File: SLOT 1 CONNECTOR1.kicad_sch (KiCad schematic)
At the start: 10 parts, among them J33 Slot1, U24 MAX1617 ME

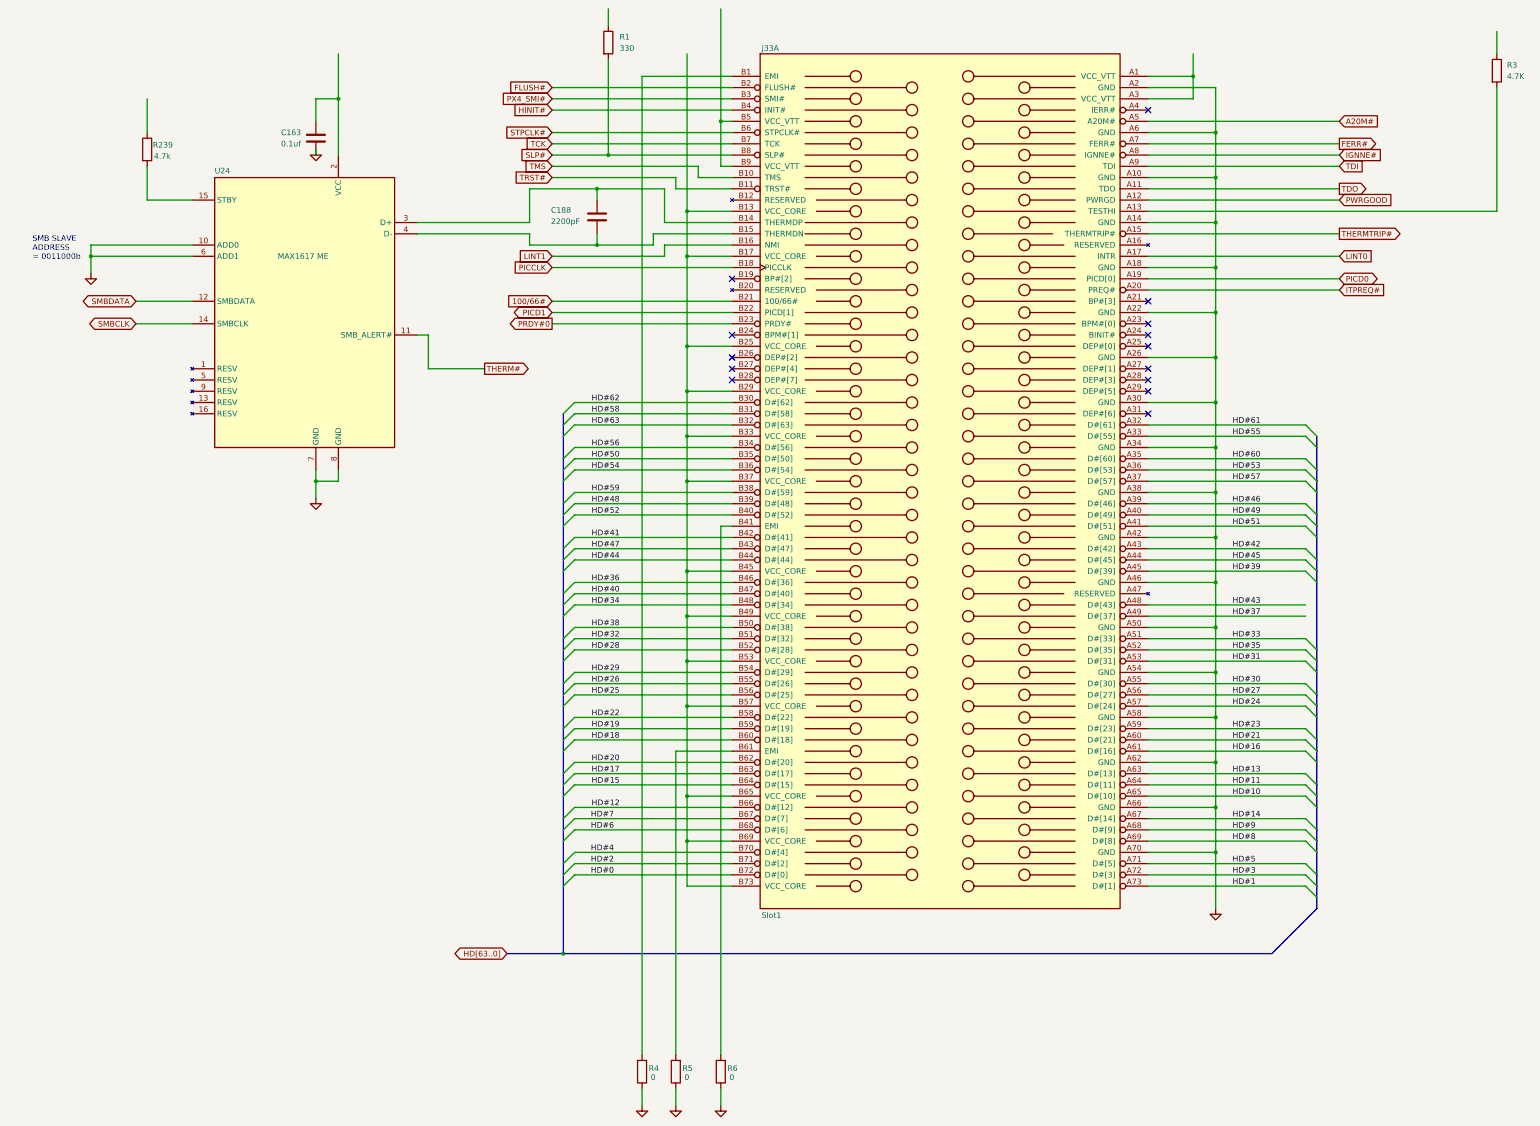
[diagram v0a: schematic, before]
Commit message: Page 3, 4 completed
perfect 1:1 symbols added: Slot1, MAX1617, Jumper
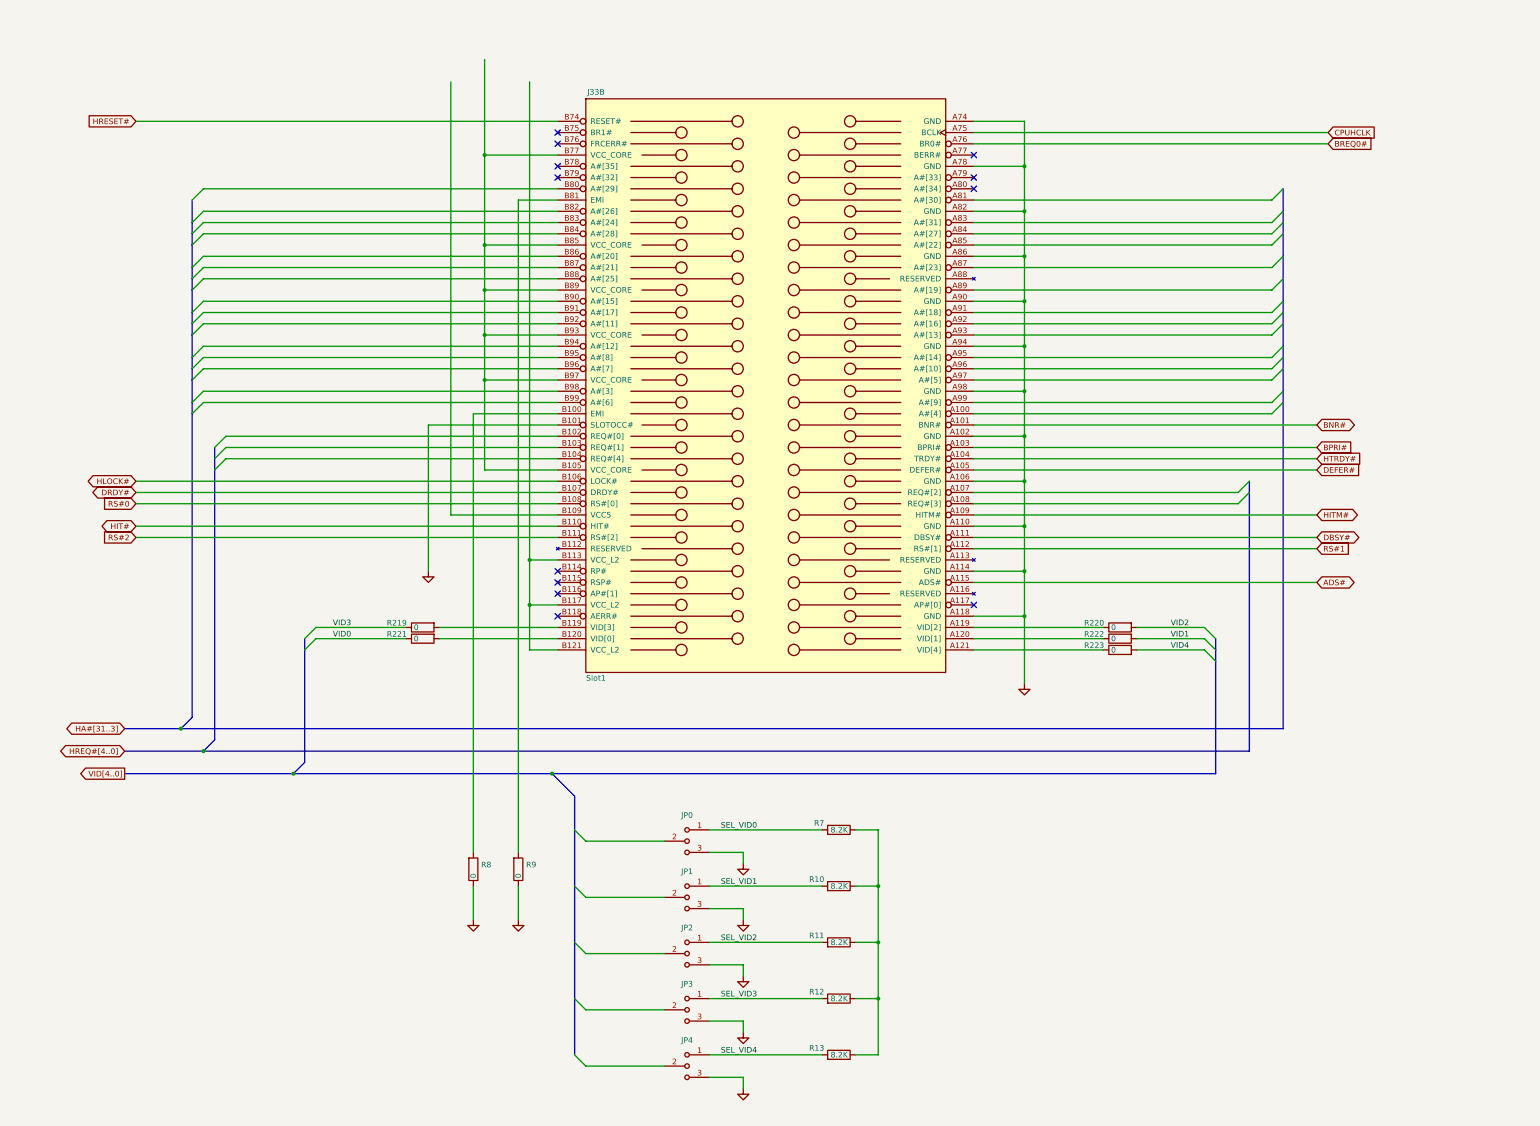
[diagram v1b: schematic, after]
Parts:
- removed C163: 0.1uf, Capacitor_SMD:C_0201_0603Metric, symbol Device:C
- removed C188: 2200pF, Capacitor_SMD:C_0201_0603Metric, symbol Device:C
- removed J33: Slot1, symbol P2-3_era:Slot1
- removed R1: 330, Resistor_SMD:R_0201_0603Metric, symbol Device:R
- removed R239: 4.7k, Resistor_SMD:R_0201_0603Metric, symbol Device:R
- removed R3: 4.7K, Resistor_SMD:R_0201_0603Metric, symbol Device:R
- removed R4, R5, R6: 0, Resistor_SMD:R_0201_0603Metric, symbol Device:R
- removed U24: MAX1617 ME, Package_SO:QSOP-16_3.9x4.9mm_P0.635mm, symbol P2-3_era:MAX1617_ME
- added J33: Slot1, symbol P2-3_era:Slot1
- added JP0, JP1, JP2, JP3, JP4: Jumper_3_Open, symbol P2-3_era:Jumper_3_Open
- added R10, R11, R12, R13, R7: 8.2K, symbol Device:R
- added R219, R220, R221, R222, R223, R8, R9: 0, Resistor_SMD:R_0201_0603Metric, symbol Device:R
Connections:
- net GND: now also J33.A102 (GND), J33.A106 (GND), J33.A110 (GND), J33.A114 (GND), J33.A118 (GND), J33.A74 (GND), J33.A78 (GND), J33.A82 (GND), J33.A86 (GND), J33.A90 (GND), J33.A94 (GND), J33.A98 (GND), J33.B101 (SLOTOCC#), JP0.3 (B), JP1.3 (B), JP2.3 (B), JP3.3 (B), JP4.3 (B), R8.1, R9.1
- new net: R10.1, R11.1, R12.1, R13.1, R7.1
- new net: J33.B119 (VID[3]), R219.2
- new net: J33.A121 (VID[4]), R223.1
- new net: J33.A119 (VID[2]), R220.1
- new net: J33.A120 (VID[1]), R222.1
- new net: J33.B100 (EMI), R8.2
- new net: J33.B105 (VCC_CORE), J33.B77 (VCC_CORE), J33.B85 (VCC_CORE), J33.B89 (VCC_CORE), J33.B93 (VCC_CORE), J33.B97 (VCC_CORE)
- new net: J33.B113 (VCC_L2), J33.B117 (VCC_L2), J33.B121 (VCC_L2)
- new net: J33.B120 (VID[0]), R221.2
- new net: J33.B81 (EMI), R9.2
- new net ADS#: J33.A115 (ADS#)
- new net BNR#: J33.A101 (BNR#)
- new net BPRI#: J33.A103 (BPRI#)
- new net BREQ0#: J33.A76 (BR0#)
- new net CPUHCLK: J33.A75 (BCLK)
- new net DBSY#: J33.A111 (DBSY#)
- new net DEFER#: J33.A105 (DEFER#)
- new net DRDY#: J33.B107 (DRDY#)
- new net HIT#: J33.B110 (HIT#)
- new net HITM#: J33.A109 (HITM#)
- new net HLOCK#: J33.B106 (LOCK#)
- new net HRESET#: J33.B74 (RESET#)
- new net HTRDY#: J33.A104 (TRDY#)
- new net RS#0: J33.B108 (RS#[0])
- new net RS#1: J33.A112 (RS#[1])
- new net RS#2: J33.B111 (RS#[2])
- new net SEL_VID0: JP0.1 (A), R7.2
- new net SEL_VID1: JP1.1 (A), R10.2
- new net SEL_VID2: JP2.1 (A), R11.2
- new net SEL_VID3: JP3.1 (A), R12.2
- new net SEL_VID4: JP4.1 (A), R13.2
- new net VID0: R221.1
- new net VID1: R222.2
- new net VID2: R220.2
- new net VID3: R219.1
- new net VID4: R223.2
- no-connect marks 14 -> 12
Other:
- note removed: "SMB SLAVE ADDRESS = 0011000b"

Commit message: page 3 4 clickable links added
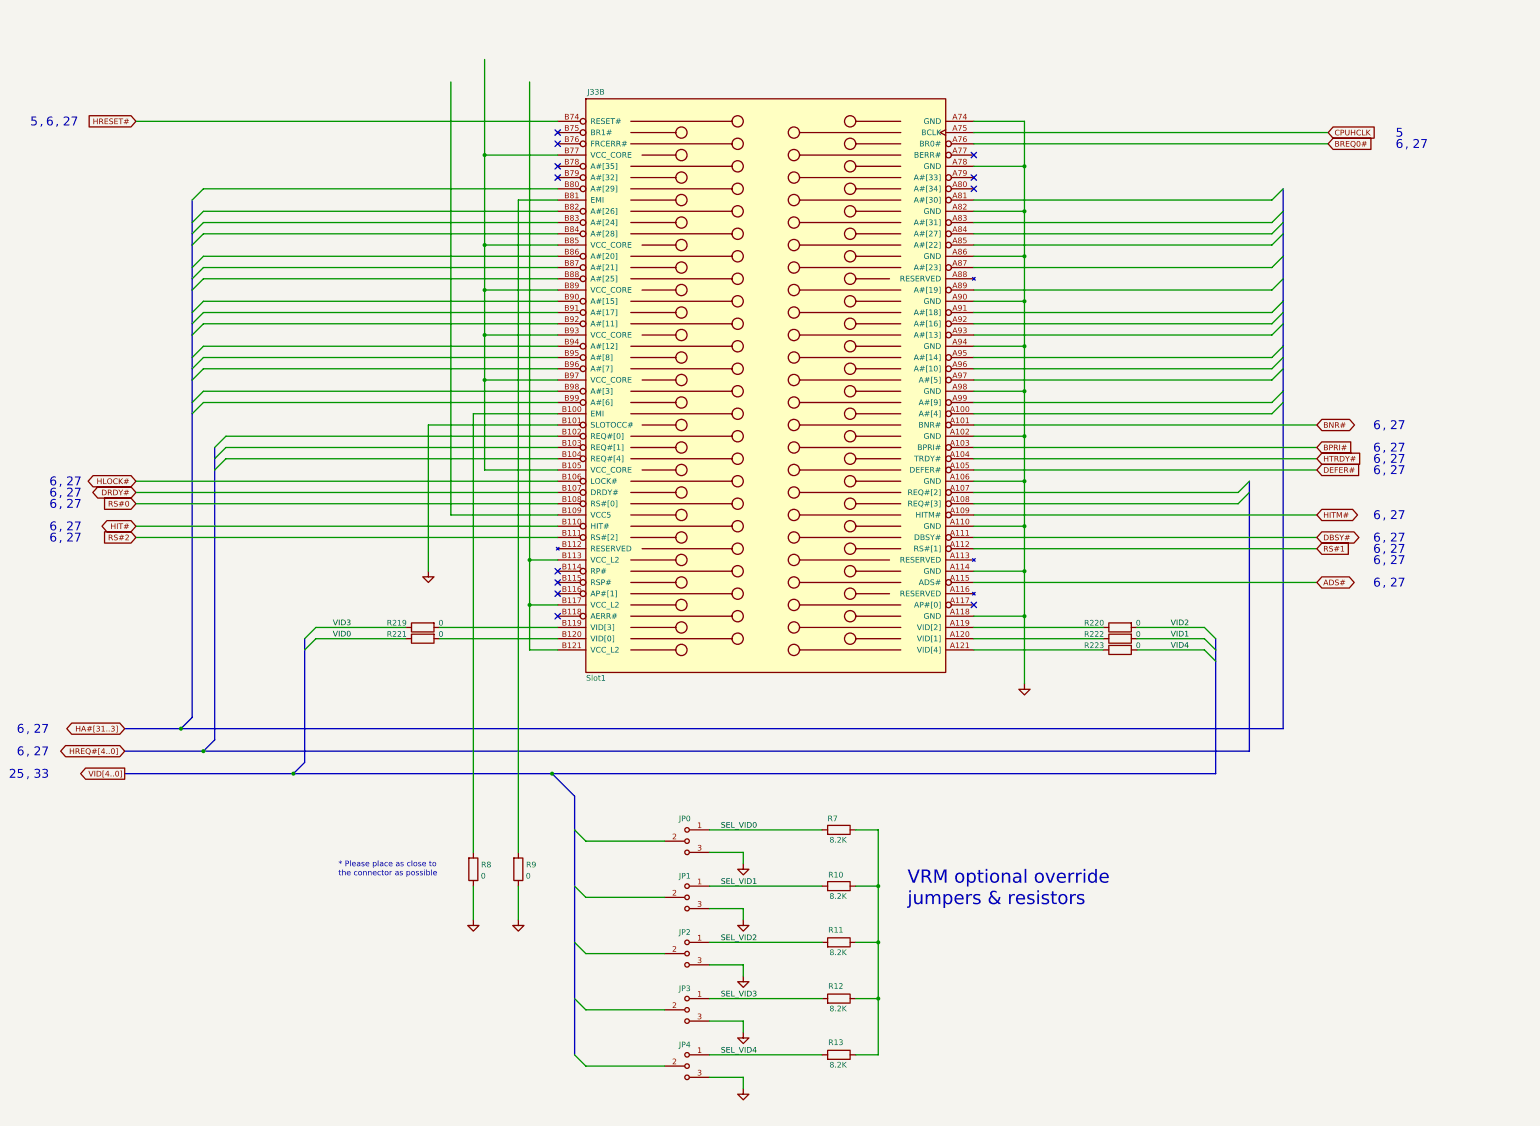
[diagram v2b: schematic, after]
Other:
- note added: "* Please place as close to the connector as possible"
- note added: ","
- note added: "25"
- note added: "27"
- note added: "33"
- note added: "5"
- note added: "6"
- note added: "VRM optional override jumpers & resistors"

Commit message: pages 9 10 11 DIMM socket and DIMM socket symbol
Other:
- title: SLOT 1 (PART I) -> SLOT 1 (PART II)
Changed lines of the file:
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@@
 	(paper "User" 380 300)
 	(title_block
-		(title "SLOT 1 (PART I)")
+		(title "SLOT 1 (PART II)")
 		(date "Thursday, April 09, 1998")
 		(rev "1.0")
@@
 		)
 		(stroke
-			(width 1)
+			(width 0.7)
 			(type default)
 		)
@@
 		)
 		(stroke
-			(width 1)
+			(width 0.7)
 			(type default)
 		)
@@
 		)
 		(stroke
-			(width 1)
+			(width 0.7)
 			(type default)
 		)
@@
 		)
 		(stroke
-			(width 1)
+			(width 0.7)
 			(type default)
 		)
@@
 		)
 		(stroke
-			(width 1)
+			(width 0.7)
 			(type default)
 		)
@@
 		)
 		(stroke
-			(width 1)
+			(width 0.7)
 			(type default)
 		)
@@
 		)
 		(stroke
-			(width 1)
+			(width 0.7)
 			(type default)
 		)
@@
 		)
 		(stroke
-			(width 1)
+			(width 0.7)
 			(type default)
 		)
@@
 		)
 		(stroke
-			(width 1)
+			(width 0.7)
 			(type default)
 		)
@@
 		)
 		(stroke
-			(width 1)
+			(width 0.7)
 			(type default)
 		)
@@
 		)
 		(stroke
-			(width 1)
+			(width 0.7)
 			(type default)
 		)
@@
 		)
 		(stroke
-			(width 1)
+			(width 0.7)
 			(type default)
 		)
@@
 		)
 		(stroke
-			(width 1)
+			(width 0.7)
 			(type default)
 		)
@@
 		)
 		(stroke
-			(width 1)
+			(width 0.7)
 			(type default)
 		)
@@
 		)
 		(stroke
-			(width 1)
+			(width 0.7)
 			(type default)
 		)
@@
 		)
 		(stroke
-			(width 1)
+			(width 0.7)
 			(type default)
 		)
@@
 		)
 		(stroke
-			(width 1)
+			(width 0.7)
 			(type default)
 		)
@@
 		)
 		(stroke
-			(width 1)
+			(width 0.7)
 			(type default)
 		)
@@
 		)
 		(stroke
-			(width 1)
+			(width 0.7)
 			(type default)
 		)
@@
 		)
 		(stroke
-			(width 1)
+			(width 0.7)
 			(type default)
 		)
@@
 		)
 		(stroke
-			(width 1)
+			(width 0.7)
 			(type default)
 		)
@@
 		)
 		(stroke
-			(width 1)
+			(width 0.7)
 			(type default)
 		)
@@
 		)
 		(stroke
-			(width 1)
+			(width 0.7)
 			(type default)
 		)
@@
 		)
 		(stroke
-			(width 1)
+			(width 0.7)
 			(type default)
 		)
@@
 		)
 		(stroke
-			(width 1)
+			(width 0.7)
 			(type default)
 		)
@@
 		)
 		(stroke
-			(width 1)
+			(width 0.7)
 			(type default)
 		)
@@
 		)
 		(stroke
-			(width 1)
+			(width 0.7)
 			(type default)
 		)
@@
 		)
 		(stroke
-			(width 1)
+			(width 0.7)
 			(type default)
 		)
@@
 		)
 		(stroke
-			(width 1)
+			(width 0.7)
 			(type default)
 		)
@@
 		)
 		(stroke
-			(width 1)
+			(width 0.7)
 			(type default)
 		)
@@
 		)
 		(stroke
-			(width 1)
+			(width 0.7)
 			(type default)
 		)
@@
 		)
 		(stroke
-			(width 1)
+			(width 0.7)
 			(type default)
 		)
@@
 		)
 		(stroke
-			(width 1)
+			(width 0.7)
 			(type default)
 		)
@@
 		)
 		(stroke
-			(width 1)
+			(width 0.7)
 			(type default)
 		)
@@
 		)
 		(stroke
-			(width 1)
+			(width 0.7)
 			(type default)
 		)
@@
 		)
 		(stroke
-			(width 1)
+			(width 0.7)
 			(type default)
 		)
@@
 		)
 		(stroke
-			(width 1)
+			(width 0.7)
 			(type default)
 		)
@@
 		)
 		(stroke
-			(width 1)
+			(width 0.7)
 			(type default)
 		)
@@
 		)
 		(stroke
-			(width 1)
+			(width 0.7)
 			(type default)
 		)
@@
 		)
 		(stroke
-			(width 1)
+			(width 0.7)
 			(type default)
 		)
@@
 		)
 		(stroke
-			(width 1)
+			(width 0.7)
 			(type default)
 		)
@@
 		)
 		(stroke
-			(width 1)
+			(width 0.7)
 			(type default)
 		)
@@
 		)
 		(stroke
-			(width 1)
+			(width 0.7)
 			(type default)
 		)
@@
 		)
 		(stroke
-			(width 1)
+			(width 0.7)
 			(type default)
 		)
@@
 		)
 		(stroke
-			(width 1)
+			(width 0.7)
 			(type default)
 		)
@@
 		)
 		(stroke
-			(width 1)
+			(width 0.7)
 			(type default)
 		)
@@
 		)
 		(stroke
-			(width 1)
+			(width 0.7)
 			(type default)
 		)
@@
 		)
 		(stroke
-			(width 1)
+			(width 0.7)
 			(type default)
 		)
@@
 		)
 		(stroke
-			(width 1)
+			(width 0.7)
 			(type default)
 		)
@@
 		)
 		(stroke
-			(width 1)
+			(width 0.7)
 			(type default)
 		)
@@
 		)
 		(stroke
-			(width 1)
+			(width 0.7)
 			(type default)
 		)
@@
 		)
 		(stroke
-			(width 1)
+			(width 0.7)
 			(type default)
 		)
@@
 		)
 		(stroke
-			(width 1)
+			(width 0.7)
 			(type default)
 		)
@@
 		)
 		(stroke
-			(width 1)
+			(width 0.7)
 			(type default)
 		)
@@
 		)
 		(stroke
-			(width 1)
-			(type default)
-		)
+			(width 0.7)
+			(type default)
+		)
